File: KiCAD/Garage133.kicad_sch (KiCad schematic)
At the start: 12 parts, among them U3 SHTC3

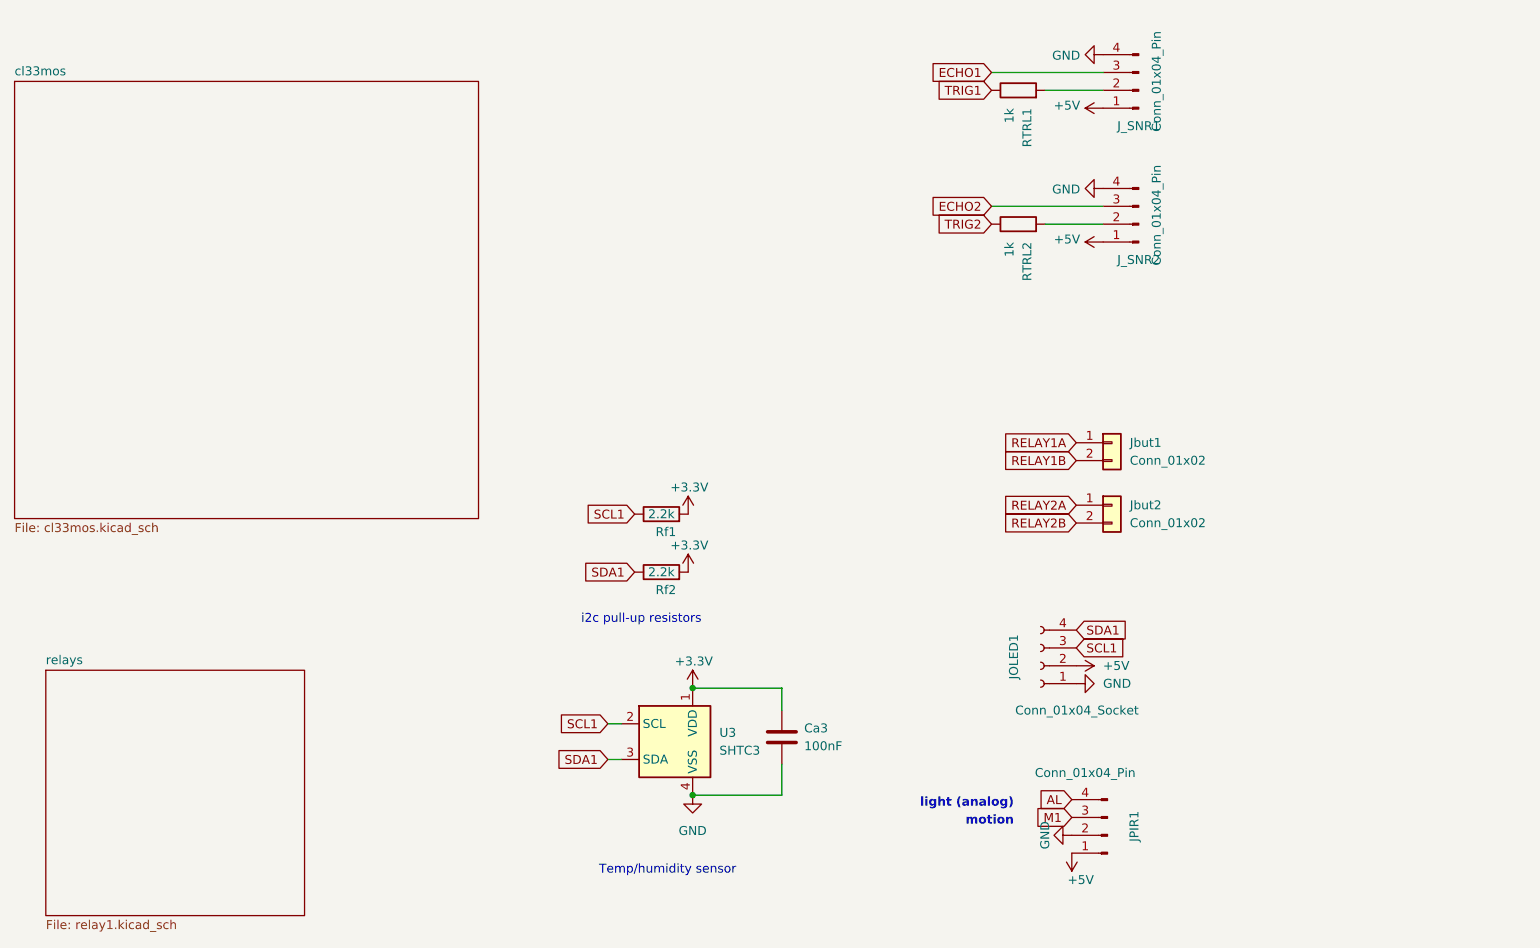
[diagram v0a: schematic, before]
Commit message: four-sonar board (#25)
The four-sonar board written about in [Dual Sonar ESP32 Garage State
Estimation](https://selectiveappeal.org/posts/garage133-dual-sonar/).

- Board supports front and back sonars for both right and left garage
bays.
- Software update for dual-observation hmm, training update.
  - Distinct states for door open with car present and not present.
- Updated ebox design, sencil fixture
- Updated device web interface
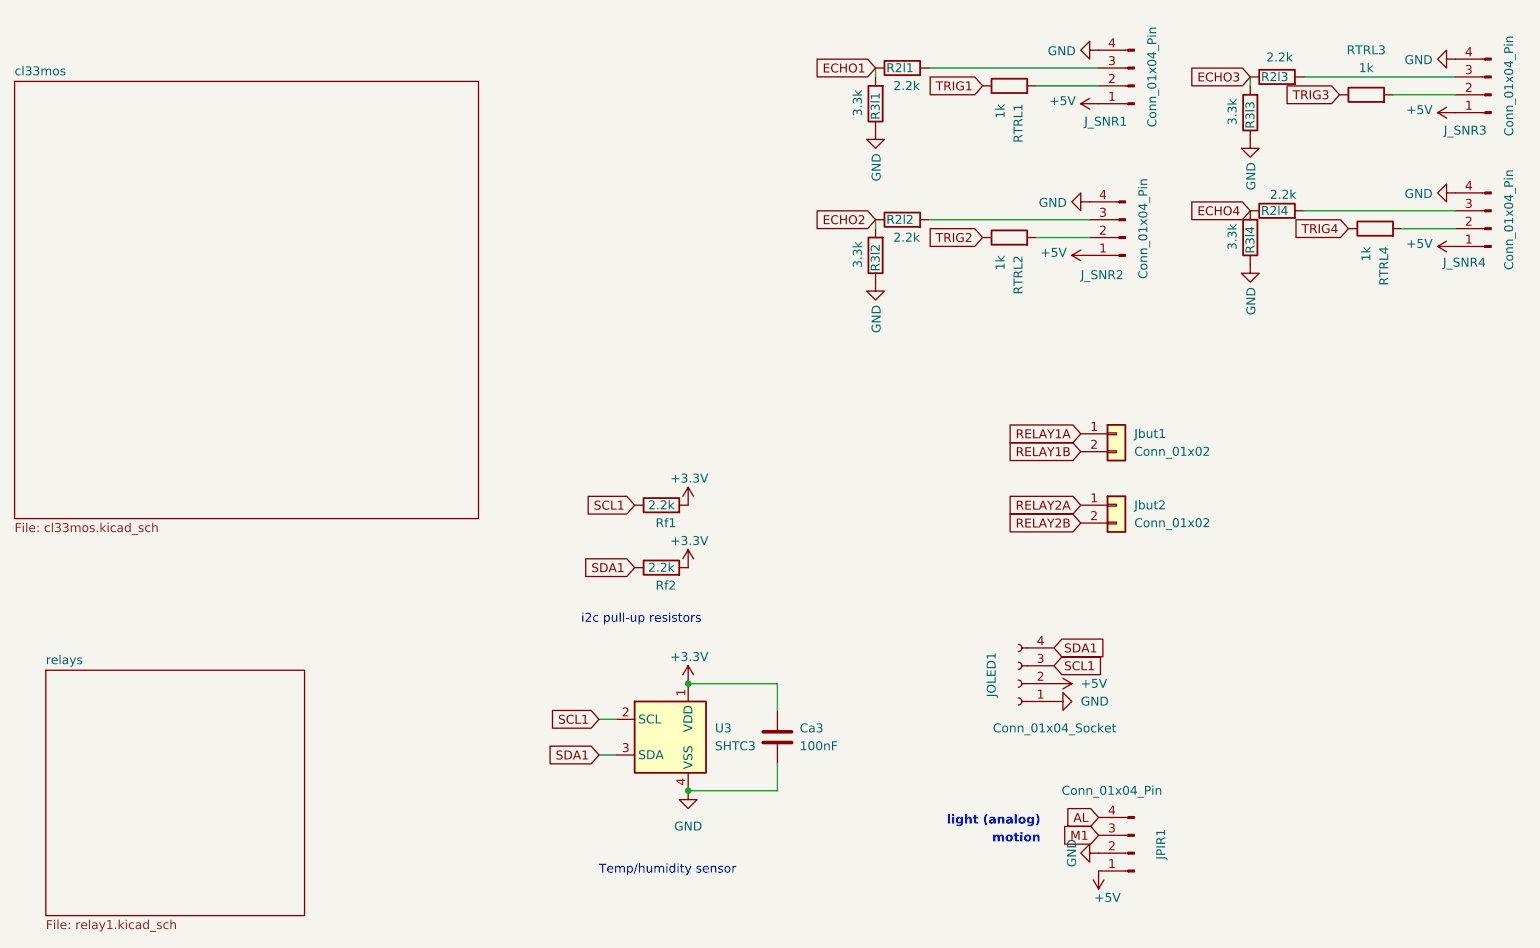
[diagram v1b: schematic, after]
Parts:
- added J_SNR3, J_SNR4: Conn_01x04_Pin, Connector_JST:JST_XH_B4B-XH-A_1x04_P2.50mm_Vertical, symbol Connector:Conn_01x04_Pin
- added R2l1, R2l2, R2l3, R2l4: 2.2k, Resistor_SMD:R_0603_1608Metric, symbol Device:R
- added R3l1, R3l2, R3l3, R3l4: 3.3k, Resistor_SMD:R_0603_1608Metric, symbol Device:R
- added RTRL3, RTRL4: 1k, Resistor_SMD:R_0603_1608Metric, symbol Device:R
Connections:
- net +5V: now also J_SNR3.1 (Pin_1), J_SNR4.1 (Pin_1)
- net ECHO1: now also R2l1.1, R3l1.2; no longer J_SNR1.3 (Pin_3)
- net ECHO2: now also R2l2.1, R3l2.2; no longer J_SNR2.3 (Pin_3)
- net GND: now also J_SNR3.4 (Pin_4), J_SNR4.4 (Pin_4), R3l1.1, R3l2.1, R3l3.1, R3l4.1
- new net: J_SNR2.3 (Pin_3), R2l2.2
- new net: J_SNR3.2 (Pin_2), RTRL3.2
- new net: J_SNR3.3 (Pin_3), R2l3.2
- new net: J_SNR4.2 (Pin_2), RTRL4.2
- new net: J_SNR4.3 (Pin_3), R2l4.2
- new net: J_SNR1.3 (Pin_3), R2l1.2
- new net ECHO3: R2l3.1, R3l3.2
- new net ECHO4: R2l4.1, R3l4.2
- new net TRIG3: RTRL3.1
- new net TRIG4: RTRL4.1
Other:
- moved on the sheet: Ca3, JOLED1, JPIR1, J_SNR1, J_SNR2, Jbut1, Jbut2, RTRL1, RTRL2, Rf1, Rf2, U3

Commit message: KiCAD board v3.0 changes (I think)
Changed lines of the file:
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@@
 			)
 		)
-		(property "Description" ""
+		(property "Description" "Resistor"
 			(at 147.32 35.56 0)
 			(effects
@@
 					(size 1.27 1.27)
 				)
+				(hide yes)
 			)
 		)
@@
 			)
 		)
-		(property "Description" ""
+		(property "Description" "Resistor"
 			(at 147.32 57.15 0)
 			(effects
@@
 					(size 1.27 1.27)
 				)
+				(hide yes)
 			)
 		)
@@
 			)
 		)
-		(property "Description" ""
+		(property "Description" "Generic connector, single row, 01x04, script generated"
 			(at 184.15 142.24 0)
 			(effects
@@
 					(size 1.27 1.27)
 				)
+				(hide yes)
 			)
 		)
@@
 			)
 		)
-		(property "Description" ""
+		(property "Description" "Generic connector, single row, 01x04, script generated"
 			(at 182.88 54.61 0)
 			(effects
@@
 					(size 1.27 1.27)
 				)
+				(hide yes)
 			)
 		)
@@
 			)
 		)
-		(property "Description" ""
+		(property "Description" "Resistor"
 			(at 116.84 92.71 0)
 			(effects
@@
 					(size 1.27 1.27)
 				)
+				(hide yes)
 			)
 		)
@@
 				(path "/42347524-93c6-40af-953e-da6b7c7bdf56"
 					(reference "#PWR032")
+					(unit 1)
+				)
+			)
+		)
+	)
+	(symbol
+		(lib_id "power:PWR_FLAG")
+		(at 120.65 133.35 0)
+		(unit 1)
+		(exclude_from_sim no)
+		(in_bom yes)
+		(on_board yes)
+		(dnp no)
+		(property "Reference" "#FLG0100"
+			(at 120.65 133.35 0)
+			(effects
+				(font
+					(size 1.27 1.27)
+				)
+				(hide yes)
+			)
+		)
+		(property "Value" "PWR_FLAG"
+			(at 120.65 133.35 0)
+			(effects
+				(font
+					(size 1.27 1.27)
+				)
+				(hide yes)
+			)
+		)
+		(property "Footprint" ""
+			(at 120.65 133.35 0)
+			(effects
+				(font
+					(size 1.27 1.27)
+				)
+			)
+		)
+		(property "Datasheet" "~"
+			(at 120.65 133.35 0)
+			(effects
+				(font
+					(size 1.27 1.27)
+				)
+			)
+		)
+		(property "Description" "Special symbol for telling ERC where power comes from"
+			(at 120.65 133.35 0)
+			(effects
+				(font
+					(size 1.27 1.27)
+				)
+				(hide yes)
+			)
+		)
+		(pin "1"
+		)
+		(instances
+			(project "Garage133"
+				(path "/42347524-93c6-40af-953e-da6b7c7bdf56"
+					(reference "#FLG0100")
 					(unit 1)
 				)
@@
 			)
 		)
-		(property "Description" ""
+		(property "Description" "Resistor"
 			(at 217.17 34.29 0)
 			(effects
@@
 					(size 1.27 1.27)
 				)
+				(hide yes)
 			)
 		)
@@
 			)
 		)
-		(property "Description" ""
+		(property "Description" "Resistor"
 			(at 200.66 54.61 0)
 			(effects
@@
 					(size 1.27 1.27)
 				)
+				(hide yes)
 			)
 		)
@@
 			)
 		)
-		(property "Description" ""
+		(property "Description" "Resistor"
 			(at 151.13 52.07 0)
 			(effects
@@
 					(size 1.27 1.27)
 				)
+				(hide yes)
 			)
 		)
@@
 			)
 		)
-		(property "Description" ""
+		(property "Description" "Generic connector, single row, 01x02, script generated (kicad-library-utils/schlib/autogen/connector/)"
 			(at 181.61 82.55 0)
 			(effects
@@
 					(size 1.27 1.27)
 				)
+				(hide yes)
 			)
 		)
@@
 			)
 		)
-		(property "Description" ""
+		(property "Description" "Resistor"
 			(at 204.47 31.75 0)
 			(effects
@@
 					(size 1.27 1.27)
 				)
+				(hide yes)
 			)
 		)
@@
 			)
 		)
-		(property "Description" ""
+		(property "Description" "Resistor"
 			(at 200.66 36.83 0)
 			(effects
@@
 					(size 1.27 1.27)
 				)
+				(hide yes)
 			)
 		)
@@
 			)
 		)
-		(property "Description" ""
+		(property "Description" "Resistor"
 			(at 218.44 53.34 0)
 			(effects
@@
 					(size 1.27 1.27)
 				)
+				(hide yes)
 			)
 		)
@@
 			)
 		)
-		(property "Description" ""
+		(property "Description" "Generic connector, single row, 01x04, script generated"
 			(at 234.95 53.34 0)
 			(effects
@@
 					(size 1.27 1.27)
 				)
+				(hide yes)
 			)
 		)
@@
 			)
 		)
-		(property "Description" ""
+		(property "Description" "Generic connector, single row, 01x04, script generated"
 			(at 184.15 33.02 0)
 			(effects
@@
 					(size 1.27 1.27)
 				)
+				(hide yes)
 			)
 		)
@@
 			)
 		)
-		(property "Description" ""
+		(property "Description" "Resistor"
 			(at 166.37 54.61 0)
 			(effects
@@
 					(size 1.27 1.27)
 				)
+				(hide yes)
 			)
 		)
@@
 			)
 		)
-		(property "Description" ""
+		(property "Description" "Generic connector, single row, 01x02, script generated (kicad-library-utils/schlib/autogen/connector/)"
 			(at 181.61 92.71 0)
 			(effects
@@
 					(size 1.27 1.27)
 				)
+				(hide yes)
 			)
 		)
@@
 			)
 		)
-		(property "Description" ""
+		(property "Description" "Resistor"
 			(at 116.84 101.6 0)
 			(effects
@@
 					(size 1.27 1.27)
 				)
+				(hide yes)
 			)
 		)
@@
 			)
 		)
-		(property "Description" ""
+		(property "Description" "Resistor"
 			(at 166.37 33.02 0)
 			(effects
@@
 					(size 1.27 1.27)
 				)
+				(hide yes)
 			)
 		)
@@
 			)
 		)
-		(property "Description" ""
+		(property "Description" "Resistor"
 			(at 151.13 30.48 0)
 			(effects
@@
 					(size 1.27 1.27)
 				)
+				(hide yes)
 			)
 		)
@@
 	)
 	(symbol
+		(lib_id "power:PWR_FLAG")
+		(at 179.07 35.56 0)
+		(unit 1)
+		(exclude_from_sim no)
+		(in_bom yes)
+		(on_board yes)
+		(dnp no)
+		(property "Reference" "#FLG0102"
+			(at 179.07 35.56 0)
+			(effects
+				(font
+					(size 1.27 1.27)
+				)
+				(hide yes)
+			)
+		)
+		(property "Value" "PWR_FLAG"
+			(at 179.07 35.56 0)
+			(effects
+				(font
+					(size 1.27 1.27)
+				)
+				(hide yes)
+			)
+		)
+		(property "Footprint" ""
+			(at 179.07 35.56 0)
+			(effects
+				(font
+					(size 1.27 1.27)
+				)
+			)
+		)
+		(property "Datasheet" "~"
+			(at 179.07 35.56 0)
+			(effects
+				(font
+					(size 1.27 1.27)
+				)
+			)
+		)
+		(property "Description" "Special symbol for telling ERC where power comes from"
+			(at 179.07 35.56 0)
+			(effects
+				(font
+					(size 1.27 1.27)
+				)
+				(hide yes)
+			)
+		)
+		(pin "1"
+		)
+		(instances
+			(project "Garage133"
+				(path "/42347524-93c6-40af-953e-da6b7c7bdf56"
+					(reference "#FLG0102")
+					(unit 1)
+				)
+			)
+		)
+	)
+	(symbol
 		(lib_id "Connector:Conn_01x04_Socket")
 		(at 167.64 118.11 180)
@@
 			)
 		)
-		(property "Description" ""
+		(property "Description" "Generic connector, single row, 01x04, script generated"
 			(at 167.64 118.11 0)
 			(effects
@@
 					(size 1.27 1.27)
 				)
+				(hide yes)
 			)
 		)
@@
 			)
 		)
-		(property "Description" ""
+		(property "Description" "Generic connector, single row, 01x04, script generated"
 			(at 234.95 34.29 0)
 			(effects
@@
 					(size 1.27 1.27)
 				)
+				(hide yes)
 			)
 		)
@@
 		)
 		(property "Value" "+3.3V"
-			(at 118.11 114.3 0)
+			(at 118.11 114.808 0)
 			(effects
 				(font
@@
 			)
 		)
-		(property "Description" ""
+		(property "Description" "Unpolarized capacitor"
 			(at 133.35 125.73 0)
 			(effects
@@
 					(size 1.27 1.27)
 				)
+				(hide yes)
 			)
 		)
@@
 			)
 		)
-		(property "Description" ""
+		(property "Description" "Resistor"
 			(at 204.47 50.8 0)
 			(effects
@@
 					(size 1.27 1.27)
 				)
-			)
-		)
+				(hide yes)
+			)
+		)

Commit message: PCB updates: board v3.1
- USB-C connect other side D+,D-
- Move USB-C to stick-out from board
- Push buttons for EN and PROG
- Move connectors away from OLED
- Move SHTC3 away from ESP32, to far side of relays. Thermal isolation milling.
- M2.5 hole for OLED support.
- Replace MMBT3906 transistors with MMBT4403 on Gemini recommendation.
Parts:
- added D_R3: YLW, LED_SMD:LED_0603_1608Metric, symbol Device:LED
- added Rl5: 1k, Resistor_SMD:R_0603_1608Metric, symbol Device:R
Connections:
- net GND: now also Rl5.1
- new net: D_R3.1 (K), Rl5.2
- new net LED1: D_R3.2 (A)
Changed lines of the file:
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@@
+		)
+	)
+	(global_label "LED1"
+		(shape input)
+		(at 222.25 88.9 180)
+		(fields_autoplaced yes)
+		(effects
+			(font
+				(size 1.27 1.27)
+			)
+			(justify right)
+		)
+		(property "Intersheetrefs" "${INTERSHEET_REFS}"
+			(at 214.6082 88.9 0)
+			(effects
+				(font
+					(size 1.27 1.27)
+				)
+				(justify right)
+				(hide yes)
+			)
 		)
 	)
@@
 	)
 	(symbol
+		(lib_id "Device:LED")
+		(at 226.06 88.9 180)
+		(unit 1)
+		(exclude_from_sim no)
+		(in_bom yes)
+		(on_board yes)
+		(dnp no)
+		(property "Reference" "D_R3"
+			(at 225.425 93.98 0)
+			(effects
+				(font
+					(size 1.27 1.27)
+				)
+				(justify right)
+			)
+		)
+		(property "Value" "YLW"
+			(at 224.79 91.44 0)
+			(effects
+				(font
+					(size 1.27 1.27)
+				)
+				(justify right)
+			)
+		)
+		(property "Footprint" "LED_SMD:LED_0603_1608Metric"
+			(at 226.06 88.9 0)
+			(effects
+				(font
+					(size 1.27 1.27)
+				)
+				(hide yes)
+			)
+		)
+		(property "Datasheet" "~"
+			(at 226.06 88.9 0)
+			(effects
+				(font
+					(size 1.27 1.27)
+				)
+				(hide yes)
+			)
+		)
+		(property "Description" "Light emitting diode"
+			(at 226.06 88.9 0)
+			(effects
+				(font
+					(size 1.27 1.27)
+				)
+				(hide yes)
+			)
+		)
+		(property "Sim.Pins" "1=K 2=A"
+			(at 226.06 88.9 0)
+			(effects
+				(font
+					(size 1.27 1.27)
+				)
+				(hide yes)
+			)
+		)
+		(pin "1"
+		)
+		(pin "2"
+		)
+		(instances
+			(project "Garage133"
+				(path "/42347524-93c6-40af-953e-da6b7c7bdf56"
+					(reference "D_R3")
+					(unit 1)
+				)
+			)
+		)
+	)
+	(symbol
 		(lib_id "Connector:Conn_01x04_Pin")
 		(at 182.88 54.61 180)
@@
 	)
 	(symbol
+		(lib_id "power:GND")
+		(at 237.49 88.9 0)
+		(unit 1)
+		(exclude_from_sim no)
+		(in_bom yes)
+		(on_board yes)
+		(dnp no)
+		(fields_autoplaced yes)
+		(property "Reference" "#PWR01"
+			(at 237.49 95.25 0)
+			(effects
+				(font
+					(size 1.27 1.27)
+				)
+				(hide yes)
+			)
+		)
+		(property "Value" "GND"
+			(at 237.49 93.98 0)
+			(effects
+				(font
+					(size 1.27 1.27)
+				)
+			)
+		)
+		(property "Footprint" ""
+			(at 237.49 88.9 0)
+			(effects
+				(font
+					(size 1.27 1.27)
+				)
+				(hide yes)
+			)
+		)
+		(property "Datasheet" ""
+			(at 237.49 88.9 0)
+			(effects
+				(font
+					(size 1.27 1.27)
+				)
+				(hide yes)
+			)
+		)
+		(property "Description" "Power symbol creates a global label with name \"GND\" , ground"
+			(at 237.49 88.9 0)
+			(effects
+				(font
+					(size 1.27 1.27)
+				)
+				(hide yes)
+			)
+		)
+		(pin "1"
+		)
+		(instances
+			(project "Garage133"
+				(path "/42347524-93c6-40af-953e-da6b7c7bdf56"
+					(reference "#PWR01")
+					(unit 1)
+				)
+			)
+		)
+	)
+	(symbol
 		(lib_id "Connector_Generic:Conn_01x02")
 		(at 181.61 82.55 0)
@@
 					(unit 1)
 				)
+			)
+		)
+	)
+	(symbol
+		(lib_id "Device:R")
+		(at 233.68 88.9 270)
+		(unit 1)
+		(exclude_from_sim no)
+		(in_bom yes)
+		(on_board yes)
+		(dnp no)
+		(fields_autoplaced yes)
+		(property "Reference" "Rl5"
+			(at 232.41 86.36 0)
+			(effects
+				(font
+					(size 1.27 1.27)
+				)
+				(justify right)
+			)
+		)
+		(property "Value" "1k"
+			(at 234.95 86.36 0)
+			(effects
+				(font
+					(size 1.27 1.27)
+				)
+				(justify right)
+			)
+		)
+		(property "Footprint" "Resistor_SMD:R_0603_1608Metric"
+			(at 233.68 87.122 90)
+			(effects
+				(font
+					(size 1.27 1.27)
+				)
+				(hide yes)
+			)
+		)
+		(property "Datasheet" "~"
+			(at 233.68 88.9 0)
+			(effects
+				(font
+					(size 1.27 1.27)
+				)
+				(hide yes)
+			)
+		)
+		(property "Description" "Resistor"
+			(at 233.68 88.9 0)
+			(effects
+				(font
+					(size 1.27 1.27)
+				)
+				(hide yes)
+			)
+		)
+		(pin "2"
+		)
+		(pin "1"
+		)
+		(instances
+			(project "Garage133"
+				(path "/42347524-93c6-40af-953e-da6b7c7bdf56"
+					(reference "Rl5")
+					(unit 1)
+				)
